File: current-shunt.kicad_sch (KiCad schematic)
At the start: 25 parts, among them J4 Conn_01x02, U7 TSR_1-2450

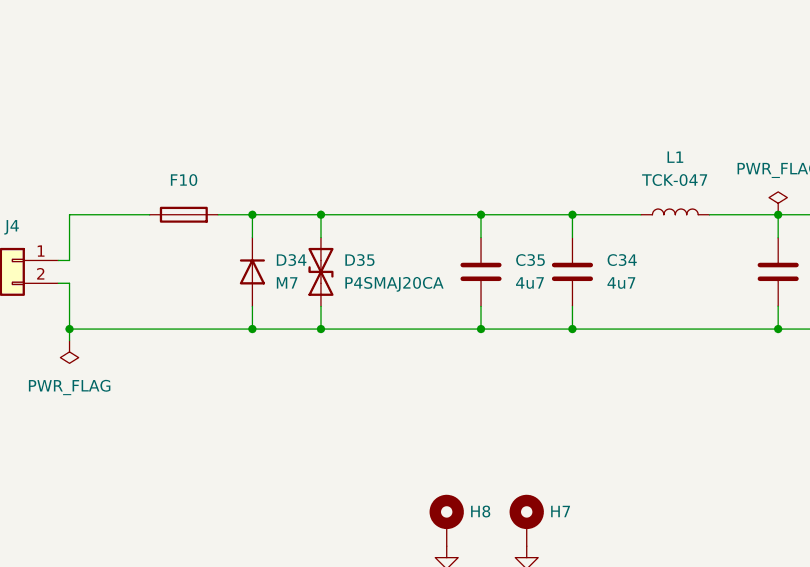
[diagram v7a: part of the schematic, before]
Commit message: Add labels to board and update not available component
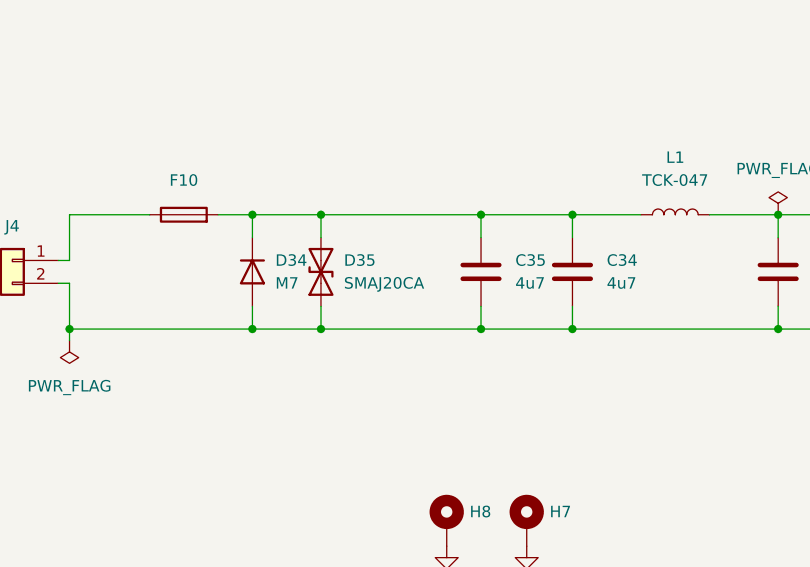
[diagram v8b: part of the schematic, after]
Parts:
- D35: value P4SMAJ20CA -> SMAJ20CA; LCSC Part # C391567 -> C309871
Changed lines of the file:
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@@
       (effects (font (size 1.27 1.27)) (justify right))
     )
-    (property "Value" "P4SMAJ20CA" (id 1) (at 146.05 140.9699 90)
+    (property "Value" "SMAJ20CA" (id 1) (at 146.05 140.9699 90)
       (effects (font (size 1.27 1.27)) (justify right))
     )
@@
       (effects (font (size 1.27 1.27)) hide)
     )
-    (property "LCSC Part #" "C391567" (id 4) (at 143.51 139.7 0)
+    (property "LCSC Part #" "C309871" (id 4) (at 143.51 139.7 0)
       (effects (font (size 1.27 1.27)) hide)
     )
@@
     )
     (path "/f44d04c5-0d17-4d52-8328-ef3b4fdfba5f/59c73eef-4962-4d24-9a04-69e3d09db436"
-      (reference "D4") (unit 1) (value "P4SMAJ20CA") (footprint "Diode_SMD:D_SMA")
+      (reference "D4") (unit 1) (value "SMAJ20CA") (footprint "Diode_SMD:D_SMA")
     )
     (path "/f44d04c5-0d17-4d52-8328-ef3b4fdfba5f/7cc5242b-a8f2-4f7d-90af-3a489294befc"
-      (reference "D5") (unit 1) (value "P4SMAJ20CA") (footprint "Diode_SMD:D_SMA")
+      (reference "D5") (unit 1) (value "SMAJ20CA") (footprint "Diode_SMD:D_SMA")
     )
     (path "/f44d04c5-0d17-4d52-8328-ef3b4fdfba5f/351b34e2-ef42-4c15-994d-be327ac81d00"
@@
     )
     (path "/f44d04c5-0d17-4d52-8328-ef3b4fdfba5f/3d87b7d0-0327-4a61-b85c-7794ea82c7dd"
-      (reference "D8") (unit 1) (value "P4SMAJ20CA") (footprint "Diode_SMD:D_SMA")
+      (reference "D8") (unit 1) (value "SMAJ20CA") (footprint "Diode_SMD:D_SMA")
     )
     (path "/f44d04c5-0d17-4d52-8328-ef3b4fdfba5f/2607000a-a698-4750-b27a-e04092e1207c"
@@
     )
     (path "/d48b6d2e-6e5f-4dac-a79e-e9dd99372c0a/59c73eef-4962-4d24-9a04-69e3d09db436"
-      (reference "D15") (unit 1) (value "P4SMAJ20CA") (footprint "Diode_SMD:D_SMA")
+      (reference "D15") (unit 1) (value "SMAJ20CA") (footprint "Diode_SMD:D_SMA")
     )
     (path "/d48b6d2e-6e5f-4dac-a79e-e9dd99372c0a/7cc5242b-a8f2-4f7d-90af-3a489294befc"
-      (reference "D16") (unit 1) (value "P4SMAJ20CA") (footprint "Diode_SMD:D_SMA")
+      (reference "D16") (unit 1) (value "SMAJ20CA") (footprint "Diode_SMD:D_SMA")
     )
     (path "/d48b6d2e-6e5f-4dac-a79e-e9dd99372c0a/351b34e2-ef42-4c15-994d-be327ac81d00"
@@
     )
     (path "/d48b6d2e-6e5f-4dac-a79e-e9dd99372c0a/3d87b7d0-0327-4a61-b85c-7794ea82c7dd"
-      (reference "D19") (unit 1) (value "P4SMAJ20CA") (footprint "Diode_SMD:D_SMA")
+      (reference "D19") (unit 1) (value "SMAJ20CA") (footprint "Diode_SMD:D_SMA")
     )
     (path "/d48b6d2e-6e5f-4dac-a79e-e9dd99372c0a/2607000a-a698-4750-b27a-e04092e1207c"
@@
     )
     (path "/34fb8779-9a92-44ba-b6c9-7eaf7f2a97bd/59c73eef-4962-4d24-9a04-69e3d09db436"
-      (reference "D26") (unit 1) (value "P4SMAJ20CA") (footprint "Diode_SMD:D_SMA")
+      (reference "D26") (unit 1) (value "SMAJ20CA") (footprint "Diode_SMD:D_SMA")
     )
     (path "/34fb8779-9a92-44ba-b6c9-7eaf7f2a97bd/7cc5242b-a8f2-4f7d-90af-3a489294befc"
-      (reference "D27") (unit 1) (value "P4SMAJ20CA") (footprint "Diode_SMD:D_SMA")
+      (reference "D27") (unit 1) (value "SMAJ20CA") (footprint "Diode_SMD:D_SMA")
     )
     (path "/34fb8779-9a92-44ba-b6c9-7eaf7f2a97bd/351b34e2-ef42-4c15-994d-be327ac81d00"
@@
     )
     (path "/34fb8779-9a92-44ba-b6c9-7eaf7f2a97bd/3d87b7d0-0327-4a61-b85c-7794ea82c7dd"
-      (reference "D30") (unit 1) (value "P4SMAJ20CA") (footprint "Diode_SMD:D_SMA")
+      (reference "D30") (unit 1) (value "SMAJ20CA") (footprint "Diode_SMD:D_SMA")
     )
     (path "/34fb8779-9a92-44ba-b6c9-7eaf7f2a97bd/2607000a-a698-4750-b27a-e04092e1207c"
@@
     )
     (path "/fa265de3-9aff-4613-b7d2-c7fb14137be3"
-      (reference "D35") (unit 1) (value "P4SMAJ20CA") (footprint "Diode_SMD:D_SMA")
+      (reference "D35") (unit 1) (value "SMAJ20CA") (footprint "Diode_SMD:D_SMA")
     )
     (path "/4395cfcd-528b-4ec6-ae6a-a96097a24238"
